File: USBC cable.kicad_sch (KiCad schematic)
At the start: 2 parts, among them J1 Conn_01x03, U1 U261-121N-4BS2S

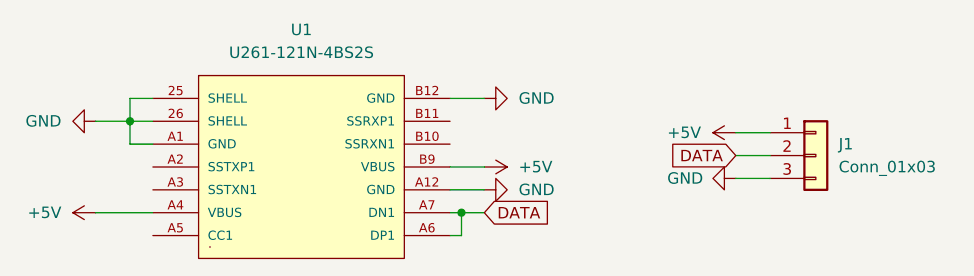
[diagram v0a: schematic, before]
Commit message: replaced small pins with large pads
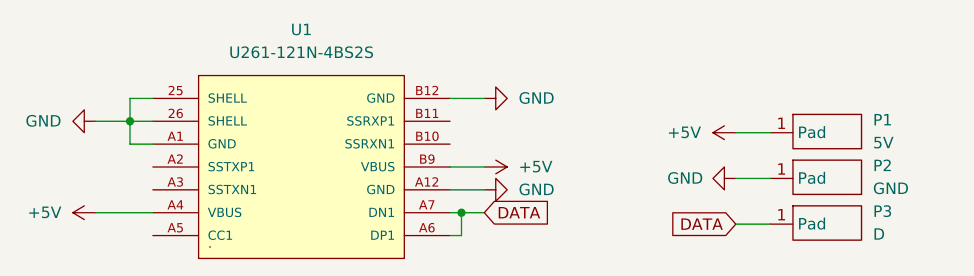
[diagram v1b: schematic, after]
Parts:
- removed J1: Conn_01x03, Connector_PinHeader_2.54mm:PinHeader_1x03_P2.54mm_Vertical, symbol Connector_Generic:Conn_01x03
- added P1: 5V, Connector:CopperField, symbol Connector:CopperField
- added P2: GND, Connector:CopperField, symbol Connector:CopperField
- added P3: D, Connector:CopperField, symbol Connector:CopperField
- U1: footprint USBCmale:U261-121N-4BS2S -> footprint:U261-121N-4BS2S
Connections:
- net +5V: now also P1.1 (Pad)
- net DATA: now also P3.1 (Pad)
- net GND: now also P2.1 (Pad)
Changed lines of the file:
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@@
     (stroke (width 0) (type default) (color 0 0 0 0))
   )
-  (wire (pts (xy 124.46 66.04) (xy 128.27 66.04))
+  (wire (pts (xy 124.46 73.66) (xy 128.27 73.66))
     (stroke (width 0) (type default) (color 0 0 0 0))
   )
@@
     )
   )
-  (global_label "DATA" (shape input) (at 124.46 66.04 180) (fields_autoplaced)
+  (global_label "DATA" (shape input) (at 124.46 73.66 180) (fields_autoplaced)
     (effects (font (size 1.27 1.27)) (justify right))
-    (property "Intersheet References" "${INTERSHEET_REFS}" (id 0) (at 117.6321 66.1194 0)
+    (property "Intersheet References" "${INTERSHEET_REFS}" (id 0) (at 117.6321 73.7394 0)
       (effects (font (size 1.27 1.27)) (justify right) hide)
     )
@@
     (pin "1")
   )
-  (symbol (lib_id "Connector_Generic:Conn_01x03") (at 133.35 66.04 0) (unit 1)
-    (in_bom yes) (on_board yes) (fields_autoplaced)
-    (property "Reference" "J1" (id 0) (at 135.89 64.7699 0)
-      (effects (font (size 1.27 1.27)) (justify left))
-    )
-    (property "Value" "Conn_01x03" (id 1) (at 135.89 67.3099 0)
-      (effects (font (size 1.27 1.27)) (justify left))
-    )
-    (property "Footprint" "Connector_PinHeader_2.54mm:PinHeader_1x03_P2.54mm_Vertical" (id 2) (at 133.35 66.04 0)
-      (effects (font (size 1.27 1.27)) hide)
-    )
-    (property "Datasheet" "~" (id 3) (at 133.35 66.04 0)
-      (effects (font (size 1.27 1.27)) hide)
-    )
-    (pin "1")
-    (pin "2")
-    (pin "3")
+  (symbol (lib_id "Connector:CopperField") (at 134.62 58.42 0) (unit 1)
+    (in_bom yes) (on_board yes) (fields_autoplaced)
+    (property "Reference" "P1" (id 0) (at 139.7 62.1029 0)
+      (effects (font (size 1.27 1.27)) (justify left))
+    )
+    (property "Value" "5V" (id 1) (at 139.7 64.6429 0)
+      (effects (font (size 1.27 1.27)) (justify left))
+    )
+    (property "Footprint" "Connector:CopperField" (id 2) (at 134.62 58.42 0)
+      (effects (font (size 1.27 1.27)) hide)
+    )
+    (property "Datasheet" "" (id 3) (at 134.62 58.42 0)
+      (effects (font (size 1.27 1.27)) hide)
+    )
+    (pin "1")
   )
   (symbol (lib_id "power:GND") (at 96.52 69.85 90) (unit 1)
@@
     )
     (property "Datasheet" "" (id 3) (at 96.52 69.85 0)
+      (effects (font (size 1.27 1.27)) hide)
+    )
+    (pin "1")
+  )
+  (symbol (lib_name "CopperField_1") (lib_id "Connector:CopperField") (at 134.62 68.58 0) (unit 1)
+    (in_bom yes) (on_board yes) (fields_autoplaced)
+    (property "Reference" "P3" (id 0) (at 139.7 72.2629 0)
+      (effects (font (size 1.27 1.27)) (justify left))
+    )
+    (property "Value" "D" (id 1) (at 139.7 74.8029 0)
+      (effects (font (size 1.27 1.27)) (justify left))
+    )
+    (property "Footprint" "Connector:CopperField" (id 2) (at 134.62 68.58 0)
+      (effects (font (size 1.27 1.27)) hide)
+    )
+    (property "Datasheet" "" (id 3) (at 134.62 68.58 0)
       (effects (font (size 1.27 1.27)) hide)
     )
@@
     (property "Reference" "U1" (id 0) (at 76.2 52.07 0))
     (property "Value" "U261-121N-4BS2S" (id 1) (at 76.2 54.61 0))
-    (property "Footprint" "USBCmale:U261-121N-4BS2S" (id 2) (at 50.8 77.47 0)
+    (property "Footprint" "footprint:U261-121N-4BS2S" (id 2) (at 50.8 77.47 0)
       (effects (font (size 1.27 1.27) italic) hide)
     )
@@
     (pin "B9")
   )
+  (symbol (lib_name "CopperField_2") (lib_id "Connector:CopperField") (at 134.62 63.5 0) (unit 1)
+    (in_bom yes) (on_board yes) (fields_autoplaced)
+    (property "Reference" "P2" (id 0) (at 139.7 67.1829 0)
+      (effects (font (size 1.27 1.27)) (justify left))
+    )
+    (property "Value" "GND" (id 1) (at 139.7 69.7229 0)
+      (effects (font (size 1.27 1.27)) (justify left))
+    )
+    (property "Footprint" "Connector:CopperField" (id 2) (at 134.62 63.5 0)
+      (effects (font (size 1.27 1.27)) hide)
+    )
+    (property "Datasheet" "" (id 3) (at 134.62 63.5 0)
+      (effects (font (size 1.27 1.27)) hide)
+    )
+    (pin "1")
+  )
   (symbol (lib_id "power:+5V") (at 124.46 63.5 90) (unit 1)
     (in_bom yes) (on_board yes)
@@
       (reference "#PWR0107") (unit 1) (value "GND") (footprint "")
     )
-    (path "/4c5af0f2-7fc3-4677-bcf0-475348ea289e"
-      (reference "J1") (unit 1) (value "Conn_01x03") (footprint "Connector_PinHeader_2.54mm:PinHeader_1x03_P2.54mm_Vertical")
+    (path "/7c507310-d715-4f1f-9c68-816d75b246e5"
+      (reference "P1") (unit 1) (value "5V") (footprint "Connector:CopperField")
+    )
+    (path "/9eef2762-3c04-43d7-9b26-d704edc052b0"
+      (reference "P2") (unit 1) (value "GND") (footprint "Connector:CopperField")
+    )
+    (path "/86122c46-0a56-4cb2-b00b-306299ff41c2"
+      (reference "P3") (unit 1) (value "D") (footprint "Connector:CopperField")
     )
     (path "/9c6abd66-0095-4a18-9ba3-57d056169b0b"
-      (reference "U1") (unit 1) (value "U261-121N-4BS2S") (footprint "USBCmale:U261-121N-4BS2S")
-    )
-  )
+      (reference "U1") (unit 1) (value "U261-121N-4BS2S") (footprint "footprint:U261-121N-4BS2S")
+    )
+  )
